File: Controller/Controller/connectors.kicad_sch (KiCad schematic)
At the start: 15 parts, among them J1 Conn_01x01_Pin, J10 Conn_01x01_Pin, J13 Conn_02x05_Odd_Even, J2 Conn_01x01_Pin, J3 Conn_01x01_Pin, J4 Conn_01x01_Pin, J5 Conn_01x01_Pin, J6 Conn_01x01_Pin, J7 Conn_01x01_Pin, J8 Conn_01x01_Pin, J9 Conn_01x01_Pin

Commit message: controller almost routed
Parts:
- added J12, J13: Conn_01x01_Pin, Connector_Pin:Pin_D1.0mm_L10.0mm, symbol Connector:Conn_01x01_Pin
- renumbered J9 to J10, J10 to J11, J1 to J2, J2 to J3, J3 to J4, J4 to J5, J5 to J6, J6 to J7, J7 to J8, J8 to J9
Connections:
- new net ISRC: J13.1 (Pin_1)
- new net KBUS: J12.1 (Pin_1)

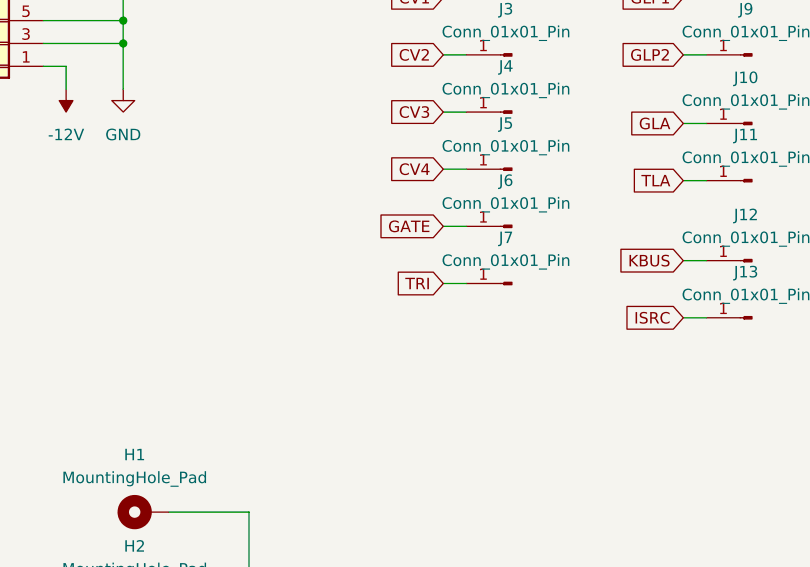
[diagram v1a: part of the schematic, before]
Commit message: controller - changed resistor sizes
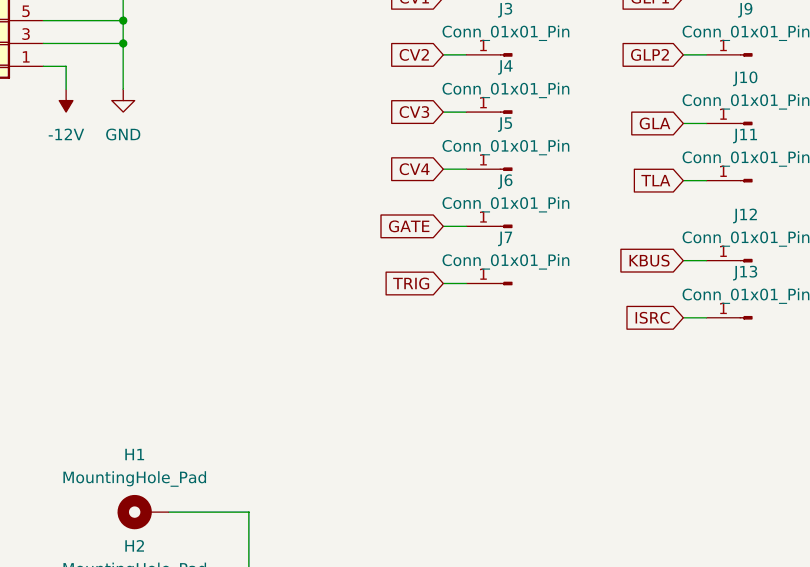
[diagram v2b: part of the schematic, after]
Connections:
- net TRI renamed TRIG
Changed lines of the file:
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@@
     )
   )
-  (global_label "TRI" (shape input) (at 105.41 88.9 180) (fields_autoplaced)
+  (global_label "TRIG" (shape input) (at 105.41 88.9 180) (fields_autoplaced)
     (effects (font (size 1.27 1.27)) (justify right))
-    (property "Intersheetrefs" "${INTERSHEET_REFS}" (at 99.5824 88.9 0)
+    (property "Intersheetrefs" "${INTERSHEET_REFS}" (at 98.3124 88.9 0)
       (effects (font (size 1.27 1.27)) (justify right) hide)
     )

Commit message: Controller - minor fixes
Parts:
- H1, H2, H3, H4, J10, J11, J12, J13, J2, J3, J4, J5, J6, J7, J8, J9: now left out of the parts list
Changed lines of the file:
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@@
   )
   (symbol (lib_id "Mechanical:MountingHole_Pad") (at 72.39 114.3 90) (unit 1)
-    (in_bom yes) (on_board yes) (dnp no) (fields_autoplaced)
+    (in_bom no) (on_board yes) (dnp no) (fields_autoplaced)
     (property "Reference" "H1" (at 71.12 107.95 90)
       (effects (font (size 1.27 1.27)))
@@
   )
   (symbol (lib_id "Connector:Conn_01x01_Pin") (at 113.03 76.2 180) (unit 1)
-    (in_bom yes) (on_board yes) (dnp no) (fields_autoplaced)
+    (in_bom no) (on_board yes) (dnp no) (fields_autoplaced)
     (property "Reference" "J5" (at 112.395 71.12 0)
       (effects (font (size 1.27 1.27)))
@@
   )
   (symbol (lib_id "Connector:Conn_01x01_Pin") (at 113.03 82.55 180) (unit 1)
-    (in_bom yes) (on_board yes) (dnp no) (fields_autoplaced)
+    (in_bom no) (on_board yes) (dnp no) (fields_autoplaced)
     (property "Reference" "J6" (at 112.395 77.47 0)
       (effects (font (size 1.27 1.27)))
@@
   )
   (symbol (lib_id "Connector:Conn_01x01_Pin") (at 139.7 71.12 180) (unit 1)
-    (in_bom yes) (on_board yes) (dnp no) (fields_autoplaced)
+    (in_bom no) (on_board yes) (dnp no) (fields_autoplaced)
     (property "Reference" "J10" (at 139.065 66.04 0)
       (effects (font (size 1.27 1.27)))
@@
   )
   (symbol (lib_id "Connector:Conn_01x01_Pin") (at 113.03 63.5 180) (unit 1)
-    (in_bom yes) (on_board yes) (dnp no) (fields_autoplaced)
+    (in_bom no) (on_board yes) (dnp no) (fields_autoplaced)
     (property "Reference" "J3" (at 112.395 58.42 0)
       (effects (font (size 1.27 1.27)))
@@
   )
   (symbol (lib_id "Connector:Conn_01x01_Pin") (at 139.7 63.5 180) (unit 1)
-    (in_bom yes) (on_board yes) (dnp no) (fields_autoplaced)
+    (in_bom no) (on_board yes) (dnp no) (fields_autoplaced)
     (property "Reference" "J9" (at 139.065 58.42 0)
       (effects (font (size 1.27 1.27)))
@@
   )
   (symbol (lib_id "Connector:Conn_01x01_Pin") (at 113.03 57.15 180) (unit 1)
-    (in_bom yes) (on_board yes) (dnp no) (fields_autoplaced)
+    (in_bom no) (on_board yes) (dnp no) (fields_autoplaced)
     (property "Reference" "J2" (at 112.395 52.07 0)
       (effects (font (size 1.27 1.27)))
@@
   )
   (symbol (lib_id "Connector:Conn_01x01_Pin") (at 139.7 77.47 180) (unit 1)
-    (in_bom yes) (on_board yes) (dnp no) (fields_autoplaced)
+    (in_bom no) (on_board yes) (dnp no) (fields_autoplaced)
     (property "Reference" "J11" (at 139.065 72.39 0)
       (effects (font (size 1.27 1.27)))
@@
   )
   (symbol (lib_id "Mechanical:MountingHole_Pad") (at 72.39 144.78 90) (unit 1)
-    (in_bom yes) (on_board yes) (dnp no) (fields_autoplaced)
+    (in_bom no) (on_board yes) (dnp no) (fields_autoplaced)
     (property "Reference" "H4" (at 71.12 138.43 90)
       (effects (font (size 1.27 1.27)))
@@
   )
   (symbol (lib_id "Connector:Conn_01x01_Pin") (at 113.03 69.85 180) (unit 1)
-    (in_bom yes) (on_board yes) (dnp no) (fields_autoplaced)
+    (in_bom no) (on_board yes) (dnp no) (fields_autoplaced)
     (property "Reference" "J4" (at 112.395 64.77 0)
       (effects (font (size 1.27 1.27)))
@@
   )
   (symbol (lib_id "Connector:Conn_01x01_Pin") (at 113.03 88.9 180) (unit 1)
-    (in_bom yes) (on_board yes) (dnp no) (fields_autoplaced)
+    (in_bom no) (on_board yes) (dnp no) (fields_autoplaced)
     (property "Reference" "J7" (at 112.395 83.82 0)
       (effects (font (size 1.27 1.27)))
@@
   )
   (symbol (lib_id "Connector:Conn_01x01_Pin") (at 139.7 57.15 180) (unit 1)
-    (in_bom yes) (on_board yes) (dnp no) (fields_autoplaced)
+    (in_bom no) (on_board yes) (dnp no) (fields_autoplaced)
     (property "Reference" "J8" (at 139.065 52.07 0)
       (effects (font (size 1.27 1.27)))
@@
   )
   (symbol (lib_id "Connector:Conn_01x01_Pin") (at 139.7 92.71 180) (unit 1)
-    (in_bom yes) (on_board yes) (dnp no) (fields_autoplaced)
+    (in_bom no) (on_board yes) (dnp no) (fields_autoplaced)
     (property "Reference" "J13" (at 139.065 87.63 0)
       (effects (font (size 1.27 1.27)))
@@
   )
   (symbol (lib_id "Mechanical:MountingHole_Pad") (at 72.39 124.46 90) (unit 1)
-    (in_bom yes) (on_board yes) (dnp no) (fields_autoplaced)
+    (in_bom no) (on_board yes) (dnp no) (fields_autoplaced)
     (property "Reference" "H2" (at 71.12 118.11 90)
       (effects (font (size 1.27 1.27)))
@@
   )
   (symbol (lib_id "Connector:Conn_01x01_Pin") (at 139.7 86.36 180) (unit 1)
-    (in_bom yes) (on_board yes) (dnp no) (fields_autoplaced)
+    (in_bom no) (on_board yes) (dnp no) (fields_autoplaced)
     (property "Reference" "J12" (at 139.065 81.28 0)
       (effects (font (size 1.27 1.27)))
@@
   )
   (symbol (lib_id "Mechanical:MountingHole_Pad") (at 72.39 134.62 90) (unit 1)
-    (in_bom yes) (on_board yes) (dnp no) (fields_autoplaced)
+    (in_bom no) (on_board yes) (dnp no) (fields_autoplaced)
     (property "Reference" "H3" (at 71.12 128.27 90)
       (effects (font (size 1.27 1.27)))
